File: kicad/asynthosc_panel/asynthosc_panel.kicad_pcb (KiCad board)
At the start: 2 copper layers, 71.1 x 128.4 mm, 24 parts, among them J15 Conn_02x04_Odd_Even

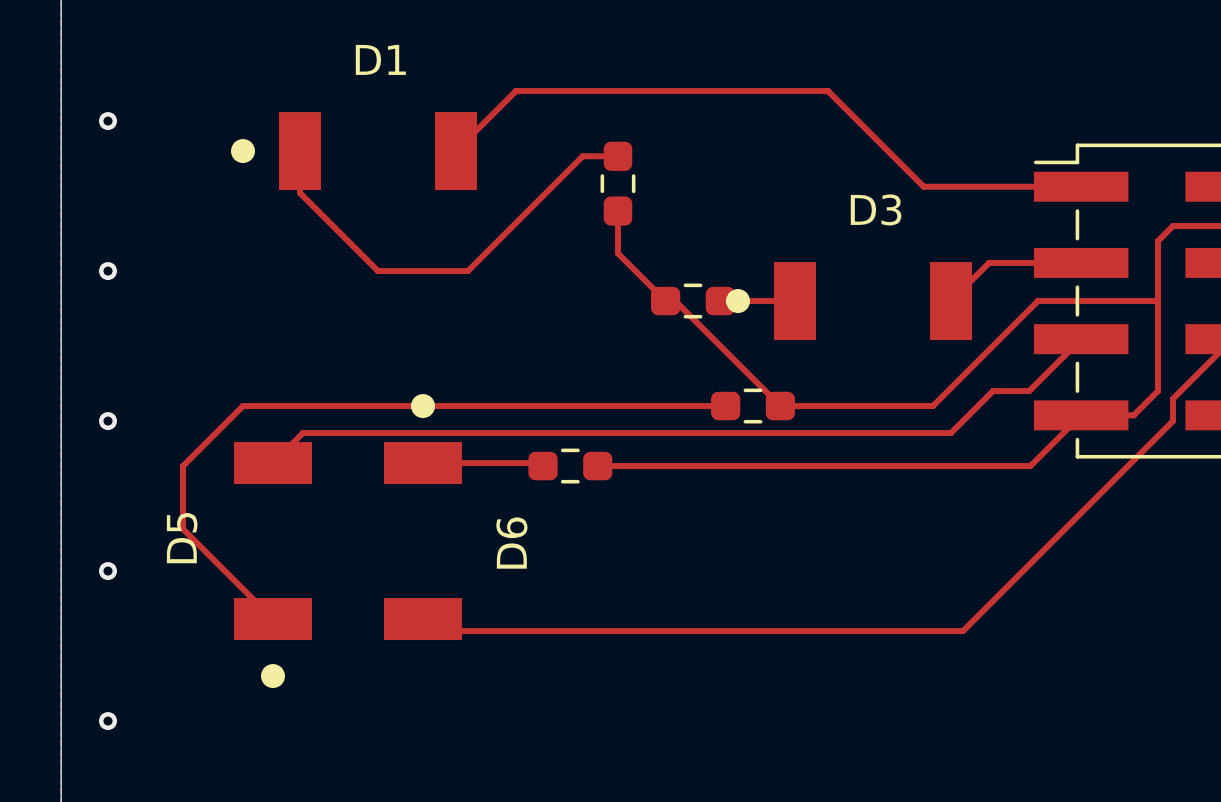
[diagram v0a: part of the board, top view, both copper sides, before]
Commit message: [FIX][PCB] Amost all DRU
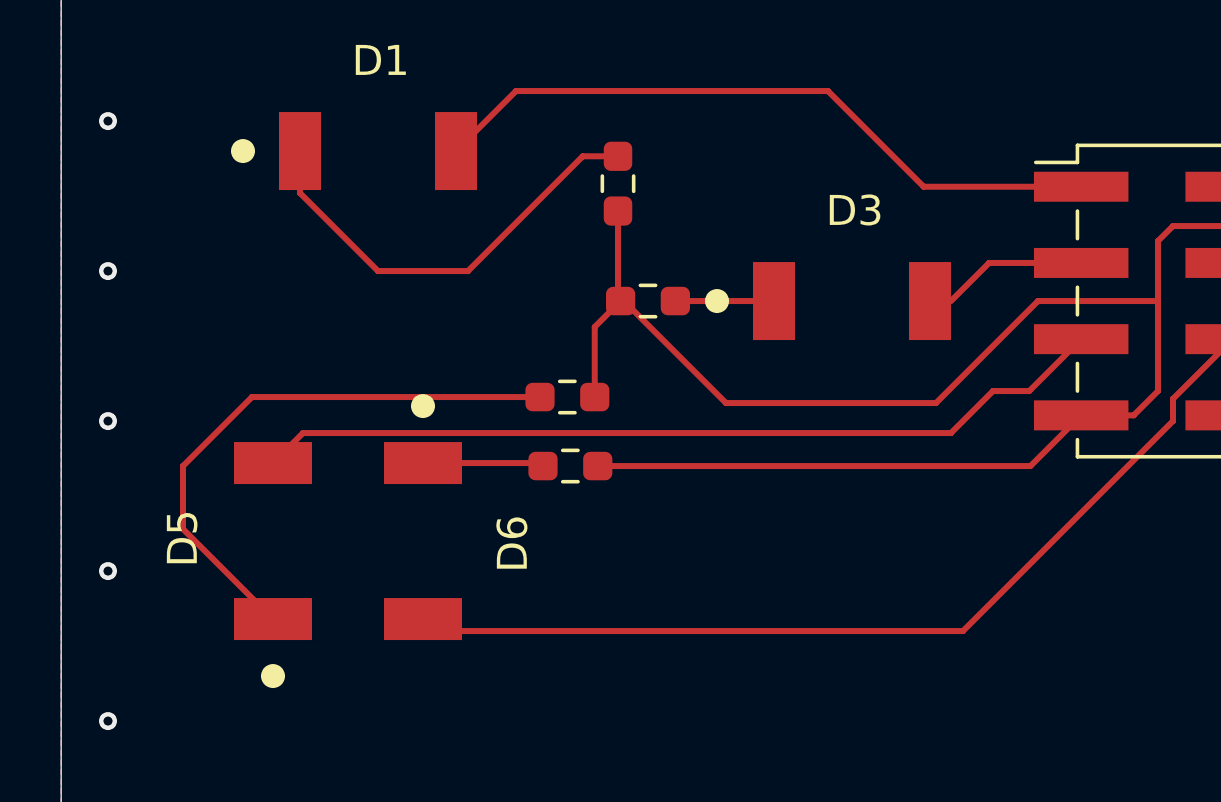
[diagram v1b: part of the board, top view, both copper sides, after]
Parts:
- moved R5 6.19 mm to (116.9, 116.2)
- moved R3 1.50 mm to (119.6, 113.0)
- moved D3 0.70 mm to (126.4, 113.0)
- moved REF** 0.20 mm to (131.6, 108.6)
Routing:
- net Net-(D5-K): track 25.2 -> 19.2 mm
- net +3V3: track 63.0 -> 67.3 mm
- net Net-(D3-K): track 2.49 -> 3.29 mm
